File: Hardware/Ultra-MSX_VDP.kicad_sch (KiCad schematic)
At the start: 4 parts, among them J3 Ultra-VDP-daughter

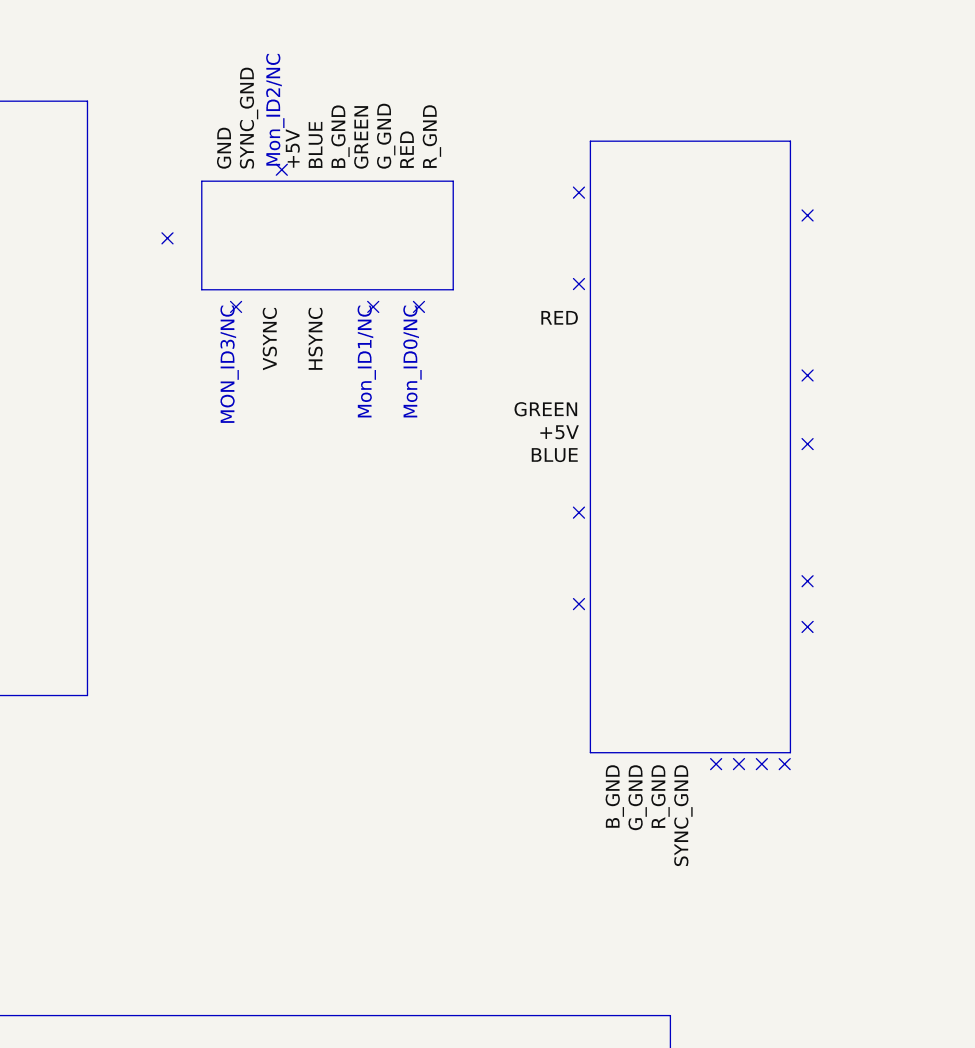
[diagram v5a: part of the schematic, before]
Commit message: Reworked the Printer-port 3D model, and the Scart 3D-model. Generated a 3D model of the main board. Moved peripheral components from separate expansion-headers, to a singular IO-shield board.
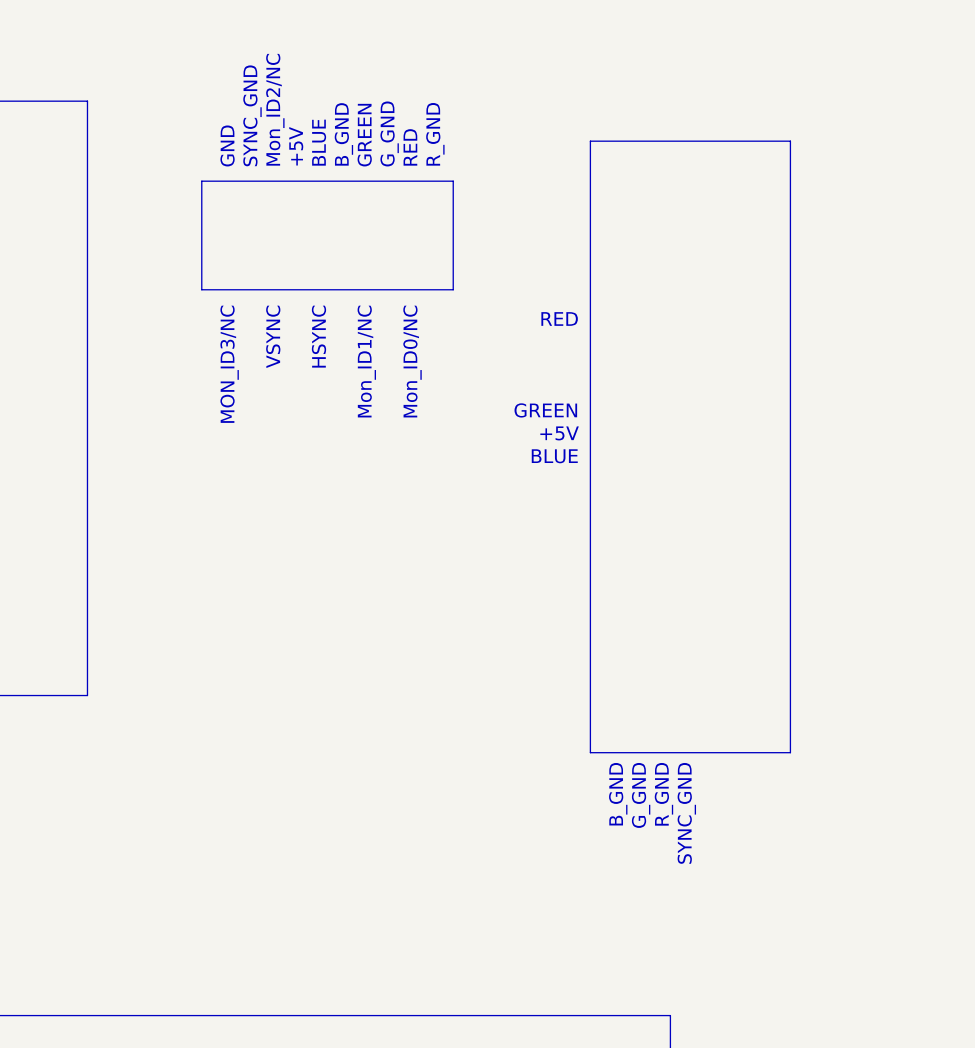
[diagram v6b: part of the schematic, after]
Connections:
- no-connect marks 18 -> 0
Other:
- note added: "+5V"
- note added: "BLUE"
- note added: "B_GND"
- note added: "GND"
- note added: "GREEN"
- note added: "G_GND"
- note added: "HSYNC"
- note added: "RED"
- note added: "R_GND"
- note added: "SYNC_GND"
- note added: "VSYNC"
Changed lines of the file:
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@@
   (junction (at 81.28 50.8) (diameter 0) (color 0 0 0 0)
   )
-  (no_connect (at 246.38 35.56))
-  (no_connect (at 292.1 40.64))
-  (no_connect (at 307.34 93.98))
-  (no_connect (at 312.42 93.98))
-  (no_connect (at 314.96 93.98))
-  (no_connect (at 292.1 66.04))
-  (no_connect (at 292.1 76.2))
-  (no_connect (at 317.5 73.66))
-  (no_connect (at 317.5 78.74))
-  (no_connect (at 292.1 30.48))
-  (no_connect (at 317.5 33.02))
-  (no_connect (at 254 43.18))
-  (no_connect (at 259.08 27.94))
-  (no_connect (at 274.32 43.18))
-  (no_connect (at 269.24 43.18))
-  (no_connect (at 309.88 93.98))
-  (no_connect (at 317.5 58.42))
-  (no_connect (at 317.5 50.8))
   (bus_entry (at 384.81 111.76) (size -2.54 2.54)
     (stroke (width 0) (type default) (color 0 0 0 0))
@@
     (effects (font (size 1.524 1.524)) (justify right bottom))
   )
+  (text "B_GND" (at 297.18 93.98 270)
+    (effects (font (size 1.524 1.524)) (justify right bottom))
+  )
+  (text "+5V" (at 261.62 27.94 90)
+    (effects (font (size 1.524 1.524)) (justify left bottom))
+  )
   (text "MON_ID3/NC" (at 254 43.18 270)
     (effects (font (size 1.524 1.524)) (justify right bottom))
   )
+  (text "GREEN" (at 292.1 55.88 180)
+    (effects (font (size 1.524 1.524)) (justify right bottom))
+  )
+  (text "RED" (at 274.32 27.94 90)
+    (effects (font (size 1.524 1.524)) (justify left bottom))
+  )
   (text "Mon_ID2/NC" (at 259.08 27.94 90)
     (effects (font (size 1.524 1.524)) (justify left bottom))
@@
     (effects (font (size 1.524 1.524)) (justify left bottom))
   )
+  (text "R_GND" (at 276.86 27.94 90)
+    (effects (font (size 1.524 1.524)) (justify left bottom))
+  )
   (text "PAL: R9 - 16k, C91 - 18pF\nR9 - Tolerance 1%" (at 386.08 269.24 0)
     (effects (font (size 1.524 1.524)) (justify left bottom))
   )
+  (text "BLUE" (at 264.16 27.94 90)
+    (effects (font (size 1.524 1.524)) (justify left bottom))
+  )
   (text "1.1. VDP-card schematic" (at 97.79 120.65 0)
     (effects (font (size 1.524 1.524)) (justify left bottom))
@@
     (effects (font (size 1.524 1.524)) (justify left bottom))
   )
+  (text "SYNC_GND" (at 304.8 93.98 270)
+    (effects (font (size 1.524 1.524)) (justify right bottom))
+  )
+  (text "G_GND" (at 271.78 27.94 90)
+    (effects (font (size 1.524 1.524)) (justify left bottom))
+  )
+  (text "SYNC_GND" (at 256.54 27.94 90)
+    (effects (font (size 1.524 1.524)) (justify left bottom))
+  )
+  (text "BLUE" (at 292.1 60.96 180)
+    (effects (font (size 1.524 1.524)) (justify right bottom))
+  )
   (text "3. SCART output" (at 182.88 19.05 0)
     (effects (font (size 1.524 1.524)) (justify left bottom))
   )
+  (text "+5V" (at 292.1 58.42 180)
+    (effects (font (size 1.524 1.524)) (justify right bottom))
+  )
+  (text "GREEN" (at 269.24 27.94 90)
+    (effects (font (size 1.524 1.524)) (justify left bottom))
+  )
   (text "1.0. Daughter-card containing Video Display Processor"
     (at 17.78 19.05 0)
     (effects (font (size 1.524 1.524)) (justify left bottom))
   )
+  (text "RED" (at 292.1 45.72 180)
+    (effects (font (size 1.524 1.524)) (justify right bottom))
+  )
   (text "2. RGB-capacitors (big)" (at 101.6 19.05 0)
     (effects (font (size 1.524 1.524)) (justify left bottom))
   )
+  (text "B_GND" (at 266.7 27.94 90)
+    (effects (font (size 1.524 1.524)) (justify left bottom))
+  )
+  (text "R_GND" (at 302.26 93.98 270)
+    (effects (font (size 1.524 1.524)) (justify right bottom))
+  )
   (text "Memory-suggestions:\n-----------------------\nModern\n----\nIS42S16100H\nIS45S16100H\n\n\nLegacy\n----"
     (at 314.325 151.13 0)
     (effects (font (size 1.524 1.524)) (justify left bottom))
   )
+  (text "VSYNC" (at 259.08 43.18 270)
+    (effects (font (size 1.524 1.524)) (justify right bottom))
+  )
   (text "JP3, JP4: 1-2: V9938; 2-3: V9958 (Use a wire link)\nJP4, JP5: 1-2: NTSC;  2-3: PAL    (Use a wire link)"
     (at 318.77 269.24 0)
@@
     (effects (font (size 1.524 1.524)) (justify left bottom))
   )
+  (text "GND" (at 254 27.94 90)
+    (effects (font (size 1.524 1.524)) (justify left bottom))
+  )
   (text "DisplayPort has a mode where it \nsends raw RGB down the wire, \nmeaning a DP to VGA converter is \n\"just\" a DAC and maybe a presence \ndetection EEPROM.\n\nExample-chip:\nPTN3356R1BSMP"
     (at 313.055 182.88 0)
@@
     (effects (font (size 1.524 1.524)) (justify left bottom))
   )
+  (text "HSYNC" (at 264.16 43.18 270)
+    (effects (font (size 1.524 1.524)) (justify right bottom))
+  )
   (text "Ultra-AV daughter-card\n" (at 142.875 31.75 0)
     (effects (font (size 1.524 1.524)) (justify left bottom))
@@
     (effects (font (size 1.524 1.524)) (justify left bottom))
   )
+  (text "G_GND" (at 299.72 93.98 270)
+    (effects (font (size 1.524 1.524)) (justify right bottom))
+  )
   (label "D7" (at 389.89 154.94 180)
     (effects (font (size 1.524 1.524)) (justify right bottom))
@@
     (effects (font (size 1.524 1.524)) (justify right bottom))
   )
-  (label "B_GND" (at 266.7 27.94 90)
-    (effects (font (size 1.524 1.524)) (justify left bottom))
-  )
   (label "VREF" (at 36.83 99.06 0)
     (effects (font (size 1.524 1.524)) (justify left bottom))
@@
     (effects (font (size 1.524 1.524)) (justify right bottom))
   )
-  (label "GREEN" (at 292.1 55.88 180)
-    (effects (font (size 1.524 1.524)) (justify right bottom))
-  )
   (label "D3" (at 389.89 144.78 180)
     (effects (font (size 1.524 1.524)) (justify right bottom))
@@
     (effects (font (size 1.524 1.524)) (justify left bottom))
   )
-  (label "G_GND" (at 271.78 27.94 90)
-    (effects (font (size 1.524 1.524)) (justify left bottom))
-  )
   (label "D4" (at 66.04 137.16 180)
     (effects (font (size 1.524 1.524)) (justify right bottom))
@@
     (effects (font (size 1.524 1.524)) (justify right bottom))
   )
-  (label "G_GND" (at 299.72 93.98 270)
-    (effects (font (size 1.524 1.524)) (justify right bottom))
-  )
   (label "CLK_VDP" (at 74.93 71.12 180)
     (effects (font (size 1.524 1.524)) (justify right bottom))
@@
     (effects (font (size 1.524 1.524)) (justify left bottom))
   )
-  (label "R_GND" (at 276.86 27.94 90)
-    (effects (font (size 1.524 1.524)) (justify left bottom))
-  )
   (label "TCK_VDP" (at 60.96 38.1 0)
     (effects (font (size 1.524 1.524)) (justify left bottom))
@@
     (effects (font (size 1.524 1.524)) (justify right bottom))
   )
-  (label "BLUE" (at 292.1 60.96 180)
-    (effects (font (size 1.524 1.524)) (justify right bottom))
-  )
   (label "ROUT" (at 382.27 189.23 0)
     (effects (font (size 1.524 1.524)) (justify left bottom))
@@
     (effects (font (size 1.524 1.524)) (justify right bottom))
   )
-  (label "GND" (at 254 27.94 90)
-    (effects (font (size 1.524 1.524)) (justify left bottom))
-  )
   (label "D0" (at 66.04 127 180)
     (effects (font (size 1.524 1.524)) (justify right bottom))
@@
     (effects (font (size 1.524 1.524)) (justify right bottom))
   )
-  (label "+5V" (at 261.62 27.94 90)
-    (effects (font (size 1.524 1.524)) (justify left bottom))
-  )
   (label "A3" (at 71.12 109.22 180)
     (effects (font (size 1.524 1.524)) (justify right bottom))
@@
     (effects (font (size 1.524 1.524)) (justify left bottom))
   )
-  (label "HSYNC" (at 264.16 43.18 270)
-    (effects (font (size 1.524 1.524)) (justify right bottom))
-  )
-  (label "R_GND" (at 302.26 93.98 270)
-    (effects (font (size 1.524 1.524)) (justify right bottom))
-  )
-  (label "SYNC_GND" (at 304.8 93.98 270)
-    (effects (font (size 1.524 1.524)) (justify right bottom))
-  )
   (label "GOUT" (at 382.27 193.04 0)
     (effects (font (size 1.524 1.524)) (justify left bottom))
@@
     (effects (font (size 1.524 1.524)) (justify right bottom))
   )
-  (label "RED" (at 292.1 45.72 180)
-    (effects (font (size 1.524 1.524)) (justify right bottom))
-  )
   (label "NTSC_CLKO" (at 74.93 66.04 180)
     (effects (font (size 1.524 1.524)) (justify right bottom))
@@
     (effects (font (size 1.524 1.524)) (justify left bottom))
   )
-  (label "B_GND" (at 297.18 93.98 270)
-    (effects (font (size 1.524 1.524)) (justify right bottom))
-  )
   (label "D10" (at 35.56 66.04 0)
     (effects (font (size 1.524 1.524)) (justify left bottom))
@@
     (effects (font (size 1.524 1.524)) (justify right bottom))
   )
-  (label "SYNC_GND" (at 256.54 27.94 90)
-    (effects (font (size 1.524 1.524)) (justify left bottom))
-  )
   (label "D9" (at 60.96 58.42 0)
     (effects (font (size 1.524 1.524)) (justify left bottom))
@@
     (effects (font (size 1.524 1.524)) (justify right bottom))
   )
-  (label "RED" (at 274.32 27.94 90)
-    (effects (font (size 1.524 1.524)) (justify left bottom))
-  )
   (label "R-Main" (at 35.56 104.14 0)
     (effects (font (size 1.524 1.524)) (justify left bottom))
@@
     (effects (font (size 1.524 1.524)) (justify right bottom))
   )
-  (label "GREEN" (at 269.24 27.94 90)
-    (effects (font (size 1.524 1.524)) (justify left bottom))
-  )
   (label "PAL_CLK_OUT" (at 378.46 79.375 0)
     (effects (font (size 1.524 1.524)) (justify left bottom))
@@
     (effects (font (size 1.524 1.524)) (justify left bottom))
   )
-  (label "VSYNC" (at 259.08 43.18 270)
-    (effects (font (size 1.524 1.524)) (justify right bottom))
-  )
   (label "A3" (at 394.97 106.68 180)
     (effects (font (size 1.524 1.524)) (justify right bottom))
   )
-  (label "+5V" (at 292.1 58.42 180)
-    (effects (font (size 1.524 1.524)) (justify right bottom))
-  )
   (label "~{VDP_WAIT}" (at 60.96 83.82 0)
     (effects (font (size 1.524 1.524)) (justify left bottom))
   )
-  (label "BLUE" (at 264.16 27.94 90)
-    (effects (font (size 1.524 1.524)) (justify left bottom))
-  )

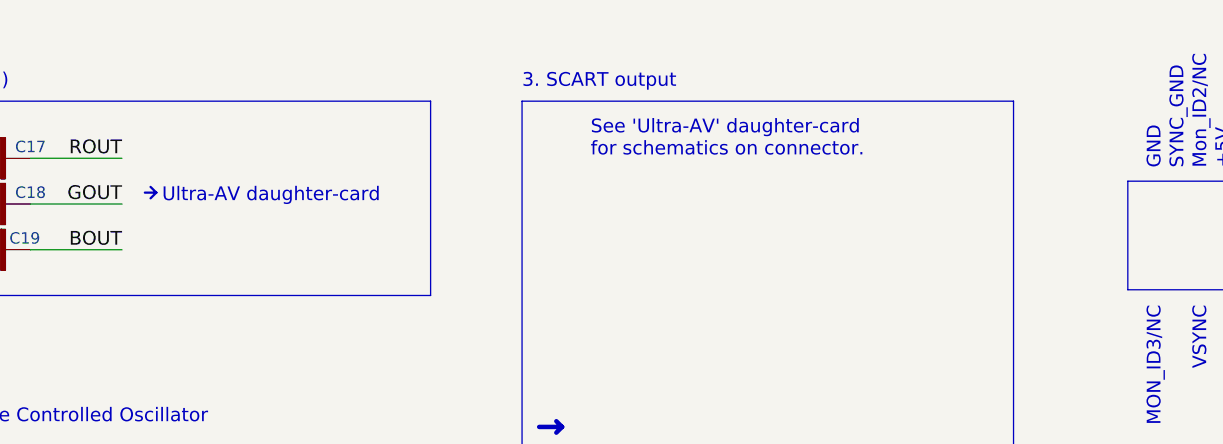
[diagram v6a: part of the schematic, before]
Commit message: Started remodelling the MSX cart-shells, as they don't seem to fit the cartridge-pcb's. Bit of clean-up in the directories.
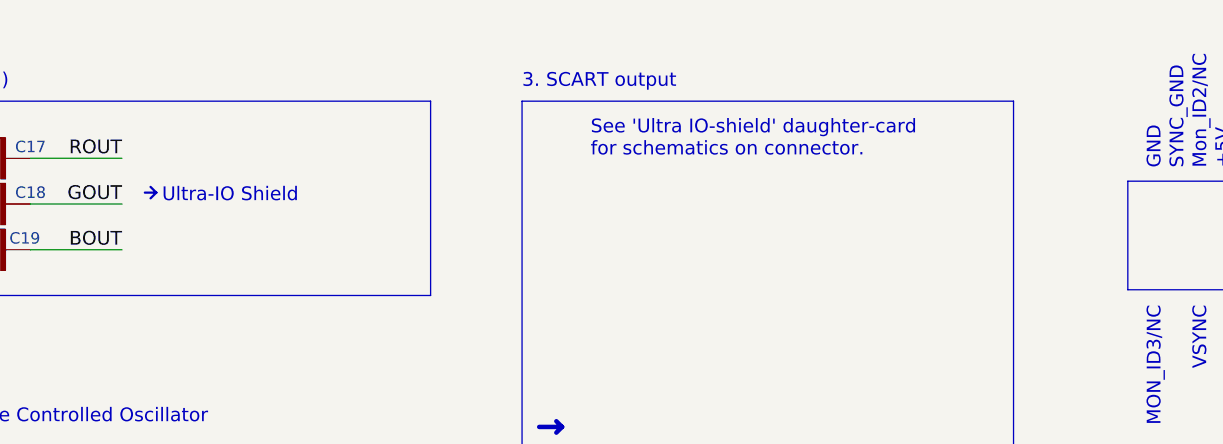
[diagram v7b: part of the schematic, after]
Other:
- note added: "See 'Ultra IO-shield' daughter-card for schematics on connector."
- note added: "Ultra-IO Shield"
- note removed: "See 'Ultra-AV' daughter-card for schematics on connector."
- note removed: "Ultra-AV daughter-card"
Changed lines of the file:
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@@
     (effects (font (size 1.524 1.524)) (justify left bottom))
   )
-  (text "See 'Ultra-AV' daughter-card \nfor schematics on connector."
+  (text "See 'Ultra IO-shield' daughter-card \nfor schematics on connector."
     (at 190.5 26.67 0)
     (effects (font (size 1.524 1.524)) (justify left bottom))
@@
     (effects (font (size 1.524 1.524)) (justify right bottom))
   )
-  (text "Ultra-AV daughter-card\n" (at 142.875 31.75 0)
+  (text "Ultra-IO Shield" (at 142.875 31.75 0)
     (effects (font (size 1.524 1.524)) (justify left bottom))
   )
